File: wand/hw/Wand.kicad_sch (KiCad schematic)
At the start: 60 parts, among them J2 Conn_01x04, J2 Conn_01x08, J3 Conn_01x08, J4 Conn_01x04, J5 USB_C_Receptacle_PowerOnly_6P, M1 Vib, Q1 Si2301, Q2 Si2302, SW1 SW_SPST, SW2 Vib, U1 SPX3819M5-L-3-3, U2 STM32G030F6Px, U3 BMI270, U4 MMC5603NJ, U5 nRF24L01P, U6 LTC4054ES5-4.2, Y1 16MHz

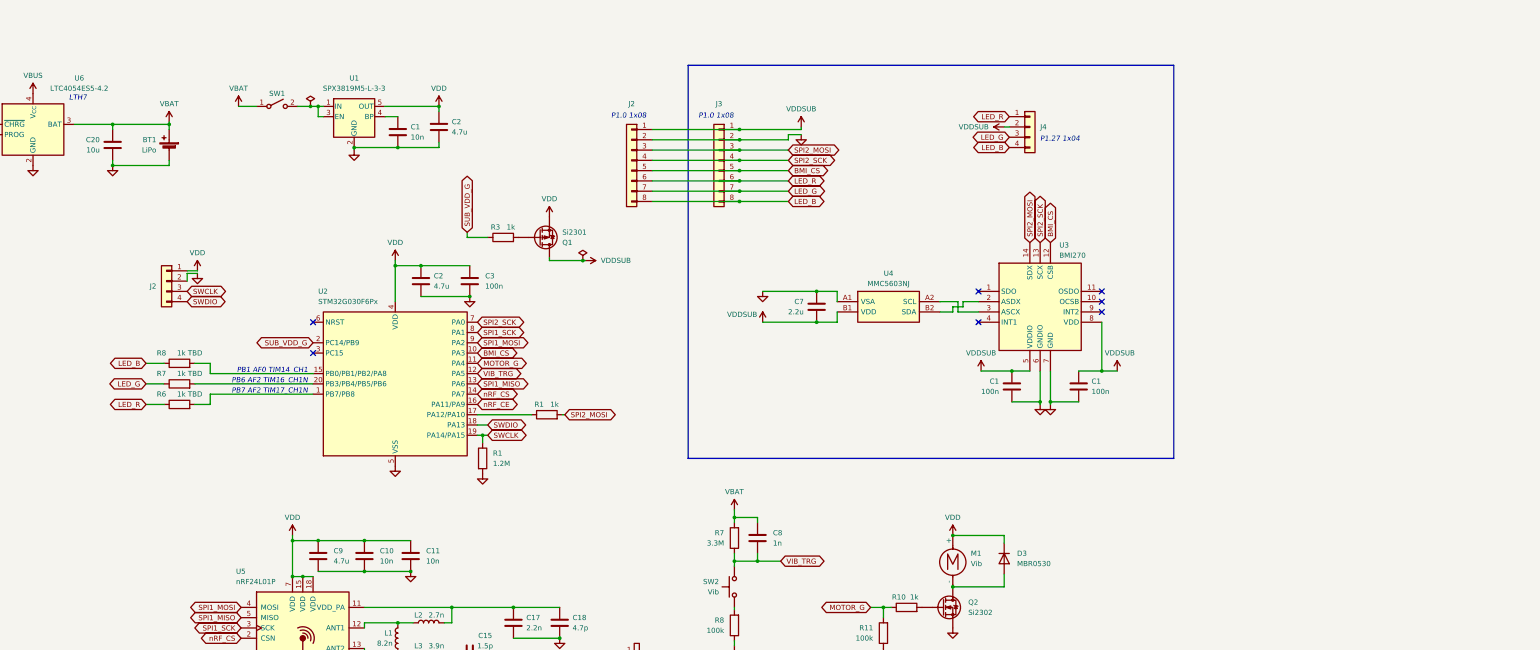
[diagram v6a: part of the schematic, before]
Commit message: 🚧 Revise schematic; use a separate MCU for the bob
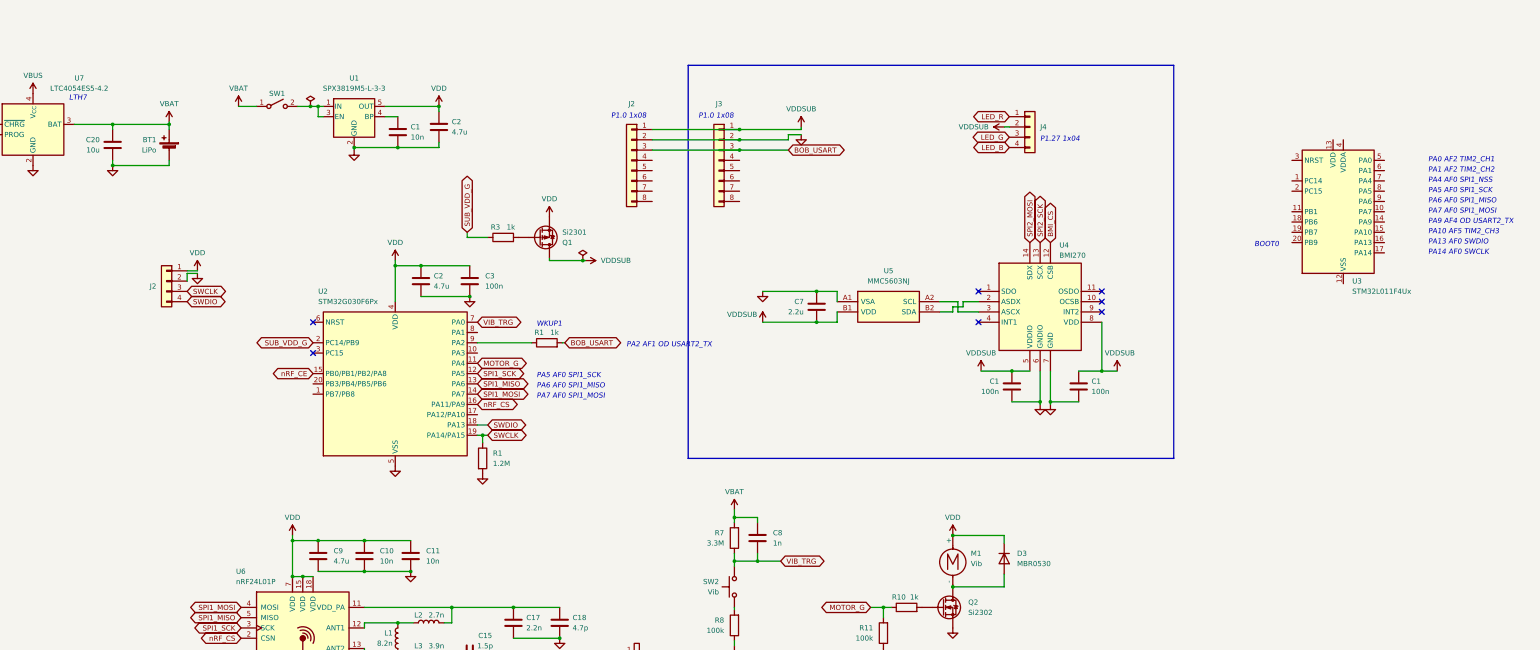
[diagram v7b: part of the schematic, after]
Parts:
- removed R6, R7, R8: 1k TBD, Resistor_SMD:R_0603_1608Metric, symbol Device:R
- added U3: STM32L011F4Ux, Package_DFN_QFN:ST_UFQFPN-20_3x3mm_P0.5mm, symbol MCU_ST_STM32L0:STM32L011F4Ux
- renumbered U3 to U4, U4 to U5, U5 to U6, U6 to U7
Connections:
- net BMI_CS: no longer J2.5 (Pin_5), J3.5 (Pin_5), U2.10 (PA3)
- net LED_B: no longer J2.8 (Pin_8), J3.8 (Pin_8)
- net LED_G: no longer J2.7 (Pin_7), J3.7 (Pin_7)
- net LED_R: no longer J2.6 (Pin_6), J3.6 (Pin_6)
- net SPI1_MOSI: now also U2.14 (PA7); no longer U2.9 (PA2)
- net SPI1_SCK: now also U2.12 (PA5); no longer U2.8 (PA1)
- net SPI2_MOSI: no longer J2.3 (Pin_3), J3.3 (Pin_3), R1.2
- net SPI2_SCK: no longer J2.4 (Pin_4), J3.4 (Pin_4), U2.7 (PA0)
- net VIB_TRG: now also U2.7 (PA0); no longer U2.12 (PA5)
- net nRF_CE: now also U2.15 (PB0/PB1/PB2/PA8); no longer U2.16 (PA11/PA9)
- net nRF_CS: now also U2.16 (PA11/PA9); no longer U2.14 (PA7)
- net at U2.17 (PA12/PA10): no longer R1.1
- new net: R1.1, U2.9 (PA2)
- new net BOB_USART: J2.3 (Pin_3), J3.3 (Pin_3), R1.2
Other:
- note added: "BOOT0"
- note added: "PA0 AF2 TIM2_CH1"
- note added: "PA1 AF2 TIM2_CH2"
- note added: "PA10 AF5 TIM2_CH3"
- note added: "PA13 AF0 SWDIO"
- note added: "PA14 AF0 SWCLK"
- note added: "PA2 AF1 OD USART2_TX"
- note added: "PA4 AF0 SPI1_NSS"
- note added: "PA5 AF0 SPI1_SCK"
- note added: "PA6 AF0 SPI1_MISO"
- note added: "PA7 AF0 SPI1_MOSI"
- note added: "PA9 AF4 OD USART2_TX"
- note added: "WKUP1"
- note removed: "PB1 AF0 TIM14_CH1"
- note removed: "PB6 AF2 TIM16_CH1N"
- note removed: "PB7 AF2 TIM17_CH1N"
- moved on the sheet: R1

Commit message: Finish revision of schematic
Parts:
- added C5: 10u, Capacitor_SMD:C_0402_1005Metric, symbol Device:C
- added C6, C7: 100n, Capacitor_SMD:C_0402_1005Metric, symbol Device:C
- added J4: Conn_01x04, Wand_footprints:TestPoints_1x04_P2.0, symbol Connector_Generic:Conn_01x04
- added R4, R5, R6: 2k TBD, Resistor_SMD:R_0603_1608Metric, symbol Device:R
- J2, J3: value Conn_01x08 -> Conn_01x03; footprint Connector_PinHeader_1.00mm:PinHeader_1x08_P1.00mm_Vertical -> Connector_PinHeader_1.00mm:PinHeader_1x03_P1.00mm_Vertical; symbol Connector_Generic:Conn_01x08 -> Connector_Generic:Conn_01x03
- renumbered C7 to C10, C8 to C11, C9 to C12, C10 to C13, C11 to C14, C12 to C15, C13 to C16, C14 to C17, C15 to C18, C16 to C19, C17 to C20, C18 to C21, C19 to C22, C20 to C23, J4 to J5, J5 to J6
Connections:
- net SPI2_MOSI is gone; now on net BMI_MOSI: U4.14 (SDX)
- net SPI2_SCK is gone; now on net BMI_SCK: U4.13 (SCX)
- net BMI_CS: now also U3.7 (PA4)
- net GND: now also U3.12 (VSS), U3.20 (PB9), C5.2, C6.2, C7.2, J4.2 (Pin_2)
- net LED_B: now also U3.15 (PA10), R6.2; no longer J5.4 (Pin_4)
- net LED_G: now also U3.6 (PA1), R5.2; no longer J5.3 (Pin_3)
- net LED_R: now also U3.5 (PA0), R4.2; no longer J5.1 (Pin_1)
- net SUB_VDD_G: now also U2.10 (PA3); no longer U2.2 (PC14/PB9)
- net VBAT: no longer C11.1, R7.2
- net VDD: now also C11.1, R7.2
- net VDDSUB: now also R1.2, U3.13 (VDD), U3.4 (VDDA), C5.1, C6.1, C7.1, J4.1 (Pin_1)
- net nRF_CE: now also U2.17 (PA12/PA10); no longer U2.15 (PB0/PB1/PB2/PA8)
- net BOB_DA: now reaches R1.1, U2.9 (PA2)
- net BOB_DA: now also J2.3 (Pin_3), J3.3 (Pin_3), U3.14 (PA9)
- net BMI_MOSI: now reaches U3.10 (PA7)
- net BSWDIO: now reaches U3.16 (PA13)
- net BSWDIO: now also J4.4 (Pin_4)
- net BSWCLK: now reaches U3.17 (PA14)
- net BSWCLK: now also J4.3 (Pin_3)
- net BMI_SCK: now reaches U3.8 (PA5)
- net BMI_MISO: now reaches U3.9 (PA6)
- net BMI_MISO: now also U4.1 (SDO)
- removed net BOB_USART: J2.3 (Pin_3), J3.3 (Pin_3), R1.2
- net SPI1_MISO renamed nRF_MISO
- net SPI1_MOSI renamed nRF_MOSI
- net SPI1_SCK renamed nRF_SCK
- net SWCLK renamed HSWCLK
- net SWDIO renamed HSWDIO
- new net: J5.1 (Pin_1), R4.1
- new net: J5.3 (Pin_3), R5.1
- new net: J5.4 (Pin_4), R6.1
- no-connect marks 9 -> 19
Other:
- note added: "P1.0 1x03"
- note added: "PA11 GP OUT"
- note added: "PA12 GP OUT"
- note added: "PA14 AF0 SWCLK / BOOT0"
- note added: "PA3 GP OUT"
- note added: "PA4 GP OUT"
- note removed: "P1.0 1x08"
- moved on the sheet: R1
